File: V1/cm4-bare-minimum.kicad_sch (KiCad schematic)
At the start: 35 parts, among them J1 Conn_01x03, J2 Conn_01x03, J3 Micro_SD_Card_Det, J4 Molex 470531000, J5 THD-20-R, J6 USB_OTG, J7 USB4105-GF-A, J8 THD-02-R, U1 EMC2301-1-ACZL-TR, U2 RT9742GGJ5, U3 74LVC1G07SE-7, U4 FSUSB42MUX, U5 MagJack-A70-112-331N126

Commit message: PCB Layout Modified to Nano-ITX
Added M.2 connector, PSU, updated PCB layout for 120mm x 120mm. Connected GPIO header. Working on remaining component and tracks placement.
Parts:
- removed D1: LED Green, LED_SMD:LED_0603_1608Metric, symbol Device:LED
- removed J6: USB_OTG, CM4IO:USB_Micro-B_EDAC_UCON00686, symbol Connector:USB_OTG
- removed J7: USB4105-GF-A, USB4105-GF-A:GCT_USB4105-GF-A, symbol USB4105-GF-A:USB4105-GF-A
- removed R1: 1k, Resistor_SMD:R_0402_1005Metric, symbol Device:R
- removed R13, R14: 5.1k, Resistor_SMD:R_0402_1005Metric, symbol Device:R
- removed U4: FSUSB42MUX, FSUSB42MUX:MSOP10_3X3_ONS, symbol FSUSB42MUX:FSUSB42MUX
- added C10, C12, C6: 10u, Capacitor_SMD:C_0805_2012Metric, symbol Device:C
- added C11, C7: 0.1u, Capacitor_SMD:C_0805_2012Metric, symbol Device:C
- added C4, C8: 1u, Capacitor_SMD:C_0805_2012Metric, symbol Device:C
- added C5: 13p, Capacitor_SMD:C_0805_2012Metric, symbol Device:C
- added C9: 10p, Capacitor_SMD:C_0805_2012Metric, symbol Device:C
- added D2: LED Green, LED_SMD:LED_0603_1608Metric, symbol Device:LED
- added D3: LED Red, LED_SMD:LED_0603_1608Metric, symbol Device:LED
- added J2: USB_OTG, CM4IO:USB_Micro-B_EDAC_UCON00686, symbol Connector:USB_OTG
- added J5: USB4105-GF-A, USB4105-GF-A:GCT_USB4105-GF-A, symbol USB4105-GF-A:USB4105-GF-A
- added J9: MDT320M03001, MDT320M03001:AMPHENOL_MDT320M03001, symbol MDT320M03001:MDT320M03001
- added L1: SRN6045TA-4R7Y, Inductor_SMD:L_Bourns_SRN6045TA, symbol pspice:INDUCTOR
- added R15: 1k, Resistor_SMD:R_0402_1005Metric, symbol Device:R
- added R19: 10, Resistor_SMD:R_0402_1005Metric, symbol Device:R
- added R2, R3: 2.2K 1%, Resistor_SMD:R_0603_1608Metric_Pad0.98x0.95mm_HandSolder, symbol Device:R
- added R20: 40.2k, Resistor_SMD:R_0402_1005Metric, symbol Device:R
- added R21: 100k, Resistor_SMD:R_0402_1005Metric, symbol Device:R
- added R22: 20k, Resistor_SMD:R_0402_1005Metric, symbol Device:R
- added R23: 13k, Resistor_SMD:R_0402_1005Metric, symbol Device:R
- added R8, R9: 5.1k, Resistor_SMD:R_0603_1608Metric_Pad0.98x0.95mm_HandSolder, symbol Device:R
- added U1: TPD2EUSB30, Package_TO_SOT_SMD:Texas_DRT-3, symbol Power_Protection:TPD2EUSB30
- added U6: MP1470, Package_TO_SOT_SMD:TSOT-23-6, symbol Regulator_Switching:MP1470
- R12: value 2.2K 1% -> 1k; Field5 9239278 -> 9239235; Field6 RK73G1ETQTP2201D -> RK73H1ETTP1001F; Field8 120889581 -> 125049511; Part Description Resistor 2.2K M1005 1% 63mW -> Resistor 1K M1005 1% 63mW
- renumbered C3 to C2, C2 to C3, D2 to D1, J4 to J1, J8 to J3, J3 to J4, J1 to J6, J2 to J7, J5 to J8, R9 to R1, R8 to R11, R11 to R13, R4 to R14, R5 to R16, R6 to R17, R7 to R18, R15 to R4, R16 to R5, R2 to R6, R3 to R7, U1 to U2, U5 to U3, U2 to U4, U3 to U5
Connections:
- net CM4_3V3: no longer D1.2 (A), R1.2
- net CM4_5V: now also C10.1, C11.1, C12.1, J5.A4_B9 (VBUS), J5.B4_A9 (VBUS__1), R21.1, U6.3 (IN)
- net GND: now also Module1.21 (PI_nLED_Activity), C10.2, C11.2, C12.2, C6.2, C7.2, C8.2, C9.2, D3.1 (K), J2.5 (GND), J2.6 (Shield), J5.A1_B12 (GND), J5.B1_A12 (GND__1), J5.SH1 (SHELL_GND), J5.SH2 (SHELL_GND__1), J5.SH3 (SHELL_GND__2), J5.SH4 (SHELL_GND__3), J9.1, J9.15, J9.21, J9.27, J9.3, J9.33, J9.39, J9.45, J9.51, J9.57, J9.69, J9.71, J9.73, J9.75, J9.9, J9.S1 (SHIELD), J9.S2 (SHIELD), R15.2, R23.2, R3.2, R8.2, R9.2, U1.3 (GND), U6.1 (GND); no longer R12.2
- net USB2_N: now also J2.2 (D-), U1.2 (D-)
- net USB2_P: now also J2.3 (D+), U1.1 (D+)
- net USB_OTG_ID: now also R2.2, R3.1; no longer R12.1
- net PCIe_CLK_nREQ: now reaches Module1.102 (PCIe_CLK_nREQ)
- net PCIe_CLK_nREQ: now also J9.52
- net PCIe_nRST: now reaches Module1.109 (PCIe_nRST)
- net PCIe_nRST: now also J9.50
- net PCIe_CLK_P: now reaches Module1.110 (PCIe_CLK_P)
- net PCIe_CLK_P: now also J9.53
- net PCIe_CLK_N: now reaches Module1.112 (PCIe_CLK_N)
- net PCIe_CLK_N: now also J9.55
- net PCIe_RX_P: now reaches Module1.116 (PCIe_RX_P)
- net PCIe_RX_P: now also J9.41
- net PCIe_RX_N: now reaches Module1.118 (PCIe_RX_N)
- net PCIe_RX_N: now also J9.43
- net PCIe_TX_P: now reaches Module1.122 (PCIe_TX_P)
- net PCIe_TX_P: now also J9.47
- net PCIe_TX_N: now reaches Module1.124 (PCIe_TX_N)
- net PCIe_TX_N: now also J9.49
- net CM4_1V8: no longer names the net of Module1.88 (+1.8v_(Output))
- net CM4_1V8: no longer Module1.90 (+1.8v_(Output))
- new net: J2.1 (VBUS), R2.1
- new net: C4.1, R19.2
- new net: C4.2, L1.1, U6.2 (SW)
- new net: J5.A5 (CC1), R8.1
- new net: J5.B5 (CC2), R9.1
- new net: D2.1 (K), R15.1
- new net: R19.1, U6.6 (BST)
- new net: C5.2, R20.2, R22.1, R23.1
- new net: R22.2, U6.4 (FB)
- new net: R21.2, U6.5 (EN)
- new net LED1: D3.2 (A), J9.10, R12.2
- new net PWR_3V3: C5.1, C6.1, C7.1, C8.1, C9.1, D1.2 (A), D2.2 (A), J9.12, J9.14, J9.16, J9.18, J9.2, J9.4, J9.70, J9.72, J9.74, L1.2, R1.2, R12.1, R20.1
- no-connect marks 82 -> 95
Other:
- note added: "3.3V @ 2A Output"
- note added: "M.2 KEY M"
- note added: "Power Supply Unit"
- note added: "USB - OTG"
- note added: "USB-C (Power Only)"
- note removed: "USB-OTG"
- moved on the sheet: C1, C2, C3, D1, J1, J3, J4, J6, J7, J8, R1, R10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

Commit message: Housekeeping, board size 120mmx40mm
V1 requirements are fulfilled, Connections are remaining in PCB layout, Performed Cleanup of repo so it only has the V1 Project.
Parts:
- removed C10, C6: 10u, Capacitor_SMD:C_0805_2012Metric, symbol Device:C
- removed C11, C7: 0.1u, Capacitor_SMD:C_0805_2012Metric, symbol Device:C
- removed C4, C8: 1u, Capacitor_SMD:C_0805_2012Metric, symbol Device:C
- removed C5: 13p, Capacitor_SMD:C_0805_2012Metric, symbol Device:C
- removed C9: 10p, Capacitor_SMD:C_0805_2012Metric, symbol Device:C
- removed D3: LED Red, LED_SMD:LED_0603_1608Metric, symbol Device:LED
- removed J8: THD-20-R, Connector_PinHeader_2.54mm:PinHeader_2x20_P2.54mm_Vertical, symbol Connector_Generic:Conn_02x20_Odd_Even
- removed J9: MDT320M03001, MDT320M03001:AMPHENOL_MDT320M03001, symbol MDT320M03001:MDT320M03001
- removed L1: SRN6045TA-4R7Y, Inductor_SMD:L_Bourns_SRN6045TA, symbol pspice:INDUCTOR
- removed R12: 1k, Resistor_SMD:R_0402_1005Metric, symbol Device:R
- removed R19: 10, Resistor_SMD:R_0402_1005Metric, symbol Device:R
- removed R20: 40.2k, Resistor_SMD:R_0402_1005Metric, symbol Device:R
- removed R21: 100k, Resistor_SMD:R_0402_1005Metric, symbol Device:R
- removed R22: 20k, Resistor_SMD:R_0402_1005Metric, symbol Device:R
- removed R23: 13k, Resistor_SMD:R_0402_1005Metric, symbol Device:R
- removed U6: MP1470, Package_TO_SOT_SMD:TSOT-23-6, symbol Regulator_Switching:MP1470
- renumbered C3 to C2, C12 to C3, C2 to C4, J4 to J3, J5 to J4, J6 to J5, J7 to J6, J3 to J7, R13 to R10, R14 to R11, R15 to R12, R16 to R13, R4 to R14, R5 to R15, R17 to R16, R18 to R17, R6 to R4, R7 to R5, R8 to R6, R9 to R7, R10 to R8, R11 to R9, U4 to U3, U5 to U4, U3 to U5
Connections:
- net TRD0_P: now also U5.1 (TRD0+)
- net AnalogIP0: no longer names the net of Module1.96 (AnalogIP0)
- net AnalogIP1: no longer names the net of Module1.94 (AnalogIP1)
- net GPIO10: no longer names the net of Module1.44 (GPIO10)
- net GPIO11: no longer names the net of Module1.38 (GPIO11)
- net GPIO12: no longer names the net of Module1.31 (GPIO12)
- net GPIO13: no longer names the net of Module1.28 (GPIO13)
- net GPIO14: no longer names the net of Module1.55 (GPIO14)
- net GPIO15: no longer names the net of Module1.51 (GPIO15)
- net GPIO16: no longer names the net of Module1.29 (GPIO16)
- net GPIO17: no longer names the net of Module1.50 (GPIO17)
- net GPIO18: no longer names the net of Module1.49 (GPIO18)
- net GPIO19: no longer names the net of Module1.26 (GPIO19)
- net GPIO2: no longer names the net of Module1.58 (GPIO2)
- net GPIO20: no longer names the net of Module1.27 (GPIO20)
- net GPIO21: no longer names the net of Module1.25 (GPIO21)
- net GPIO22: no longer names the net of Module1.46 (GPIO22)
- net GPIO23: no longer names the net of Module1.47 (GPIO23)
- net GPIO24: no longer names the net of Module1.45 (GPIO24)
- net GPIO25: no longer names the net of Module1.41 (GPIO25)
- net GPIO26: no longer names the net of Module1.24 (GPIO26)
- net GPIO27: no longer names the net of Module1.48 (GPIO27)
- net GPIO3: no longer names the net of Module1.56 (GPIO3)
- net GPIO4: no longer names the net of Module1.54 (GPIO4)
- net GPIO5: no longer names the net of Module1.34 (GPIO5)
- net GPIO6: no longer names the net of Module1.30 (GPIO6)
- net GPIO7: no longer names the net of Module1.37 (GPIO7)
- net GPIO8: no longer names the net of Module1.39 (GPIO8)
- net GPIO9: no longer names the net of Module1.40 (GPIO9)
- net ID_SC: no longer names the net of Module1.35 (ID_SC)
- net ID_SD: no longer names the net of Module1.36 (ID_SD)
- net PCIe_CLK_N: no longer names the net of Module1.112 (PCIe_CLK_N)
- net PCIe_CLK_P: no longer names the net of Module1.110 (PCIe_CLK_P)
- net PCIe_CLK_nREQ: no longer names the net of Module1.102 (PCIe_CLK_nREQ)
- net PCIe_RX_N: no longer names the net of Module1.118 (PCIe_RX_N)
- net PCIe_RX_P: no longer names the net of Module1.116 (PCIe_RX_P)
- net PCIe_TX_N: no longer names the net of Module1.124 (PCIe_TX_N)
- net PCIe_TX_P: no longer names the net of Module1.122 (PCIe_TX_P)
- net PCIe_nRST: no longer names the net of Module1.109 (PCIe_nRST)
- no-connect marks 95 -> 118
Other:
- note removed: "3.3V @ 2A Output"
- note removed: "40Way GPIO Header"
- note removed: "M.2 KEY M"
- note removed: "Power Supply Unit"
- moved on the sheet: C1, C2, C3, C4, D1, D2, J1, J2, J3, J4, J5, J6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

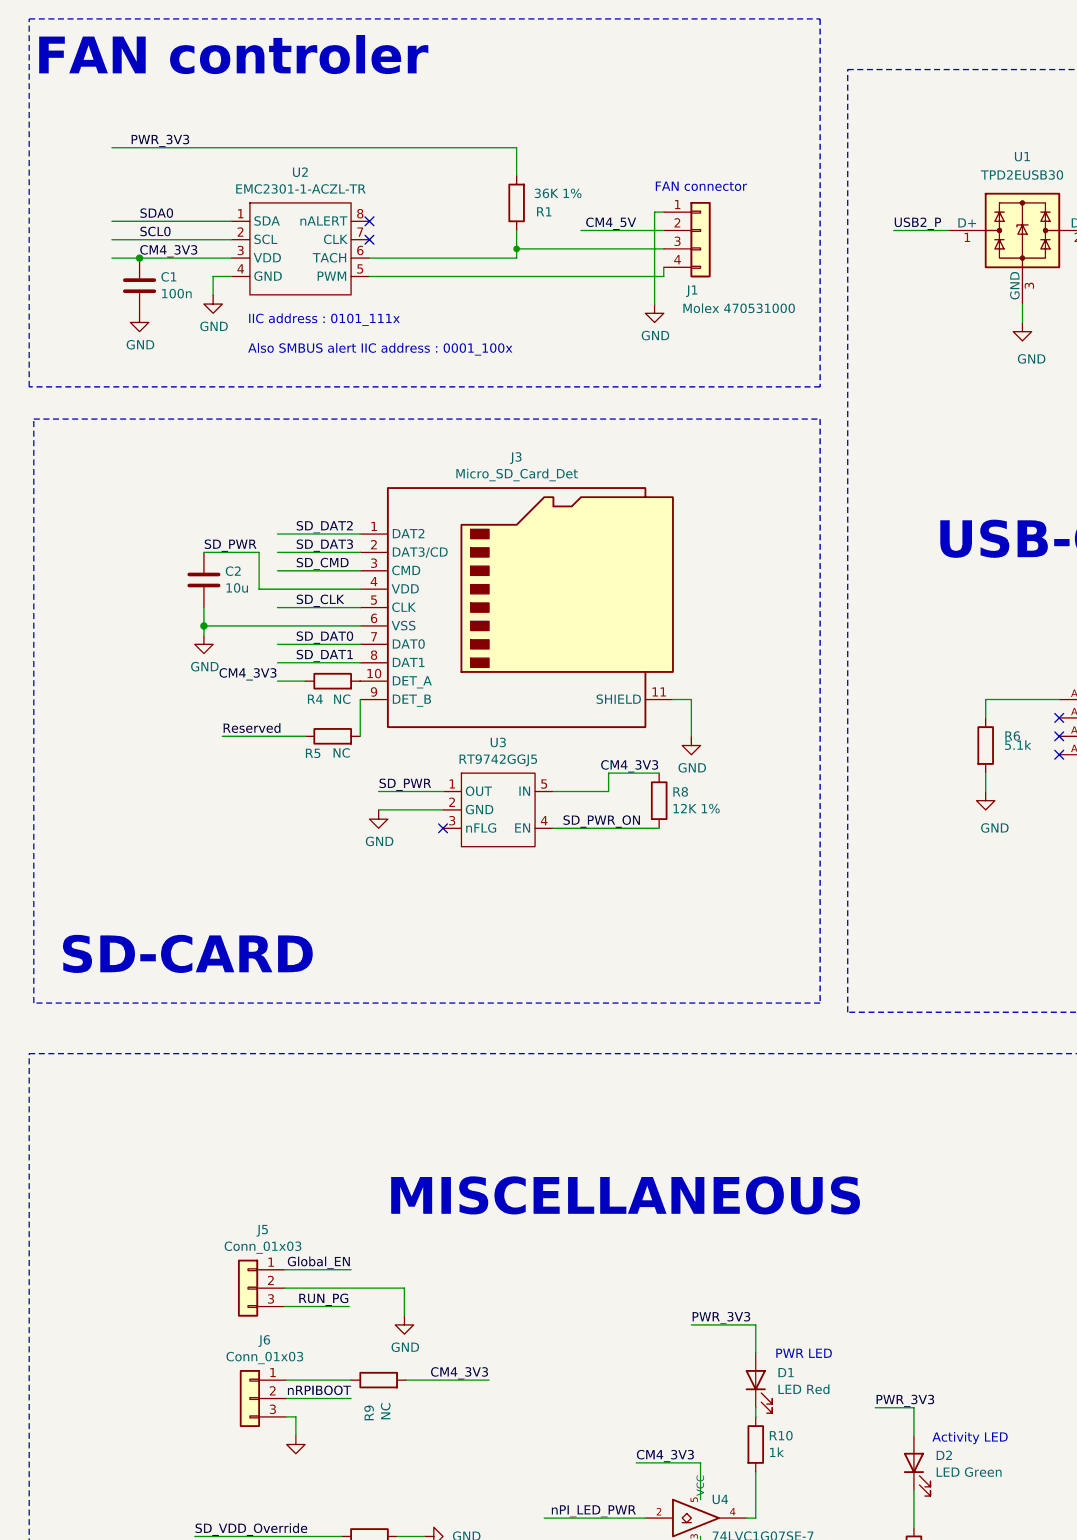
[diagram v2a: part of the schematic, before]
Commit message: Fixed Typo in Schematic
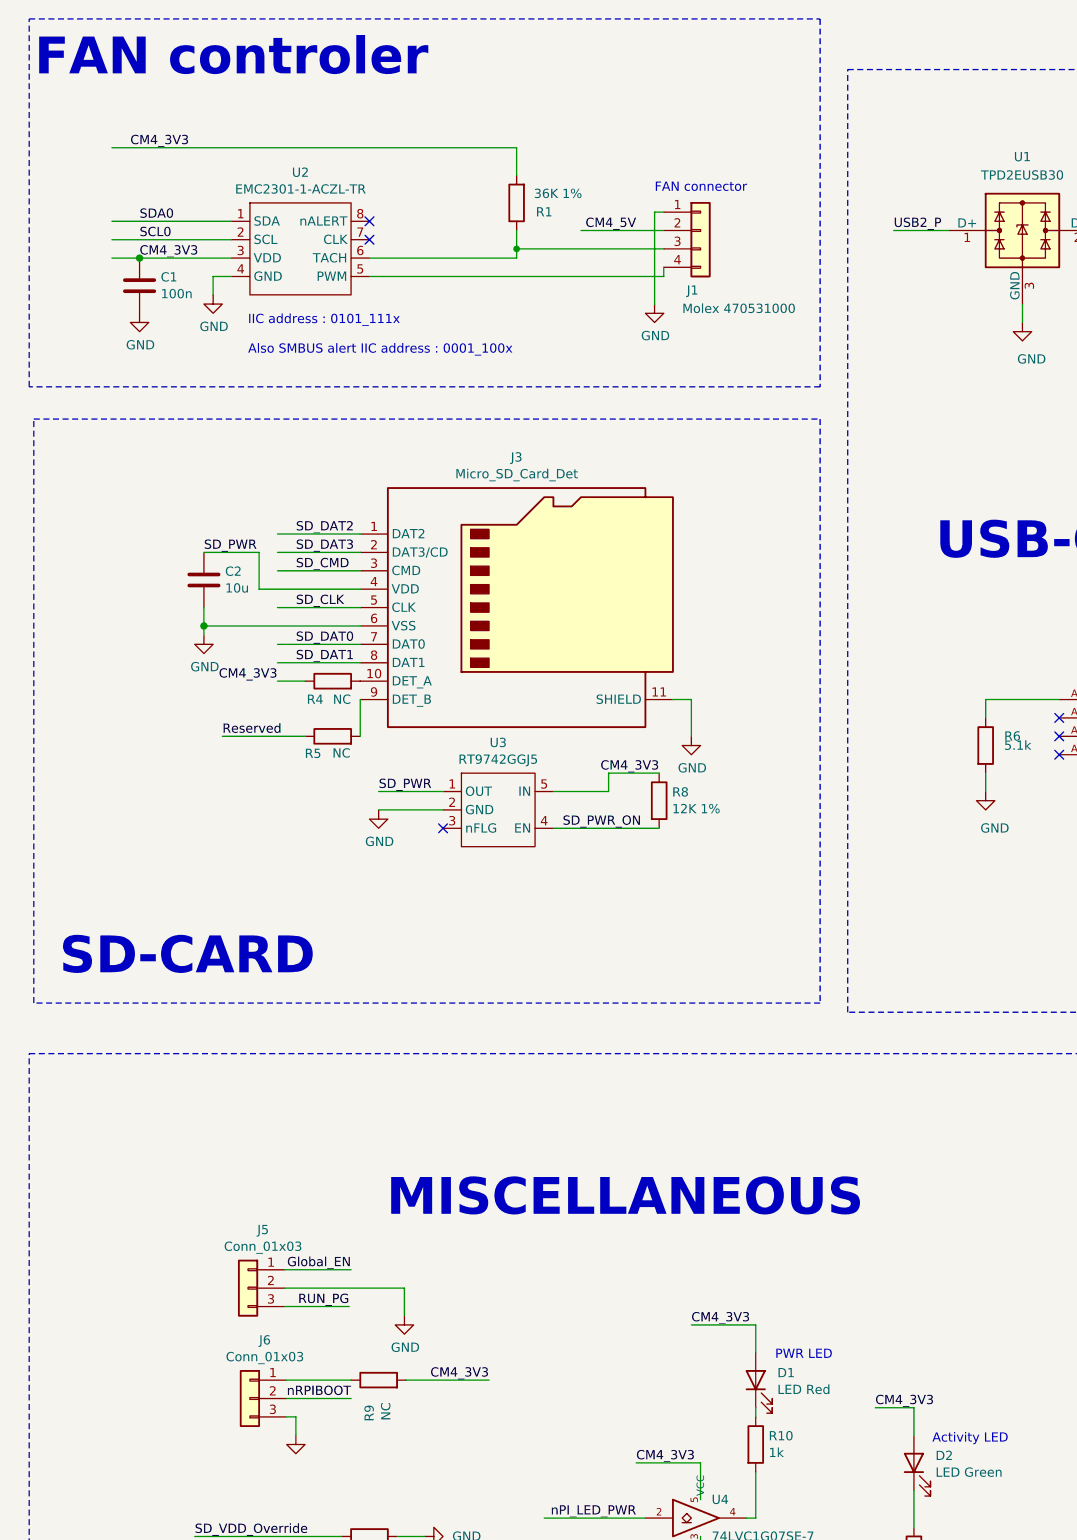
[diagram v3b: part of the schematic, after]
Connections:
- net PWR_3V3 is gone; now on net CM4_3V3: D1.2 (A), D2.2 (A), R1.2
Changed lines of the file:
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@@
 		)
 	)
-	(label "PWR_3V3"
+	(label "CM4_3V3"
 		(at 365.76 228.6 0)
 		(fields_autoplaced yes)
@@
 		)
 	)
-	(label "PWR_3V3"
+	(label "CM4_3V3"
 		(at 262.89 54.61 0)
 		(fields_autoplaced yes)
@@
 		)
 	)
-	(label "PWR_3V3"
+	(label "CM4_3V3"
 		(at 340.36 217.17 0)
 		(fields_autoplaced yes)
